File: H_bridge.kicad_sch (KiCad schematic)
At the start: 42 parts

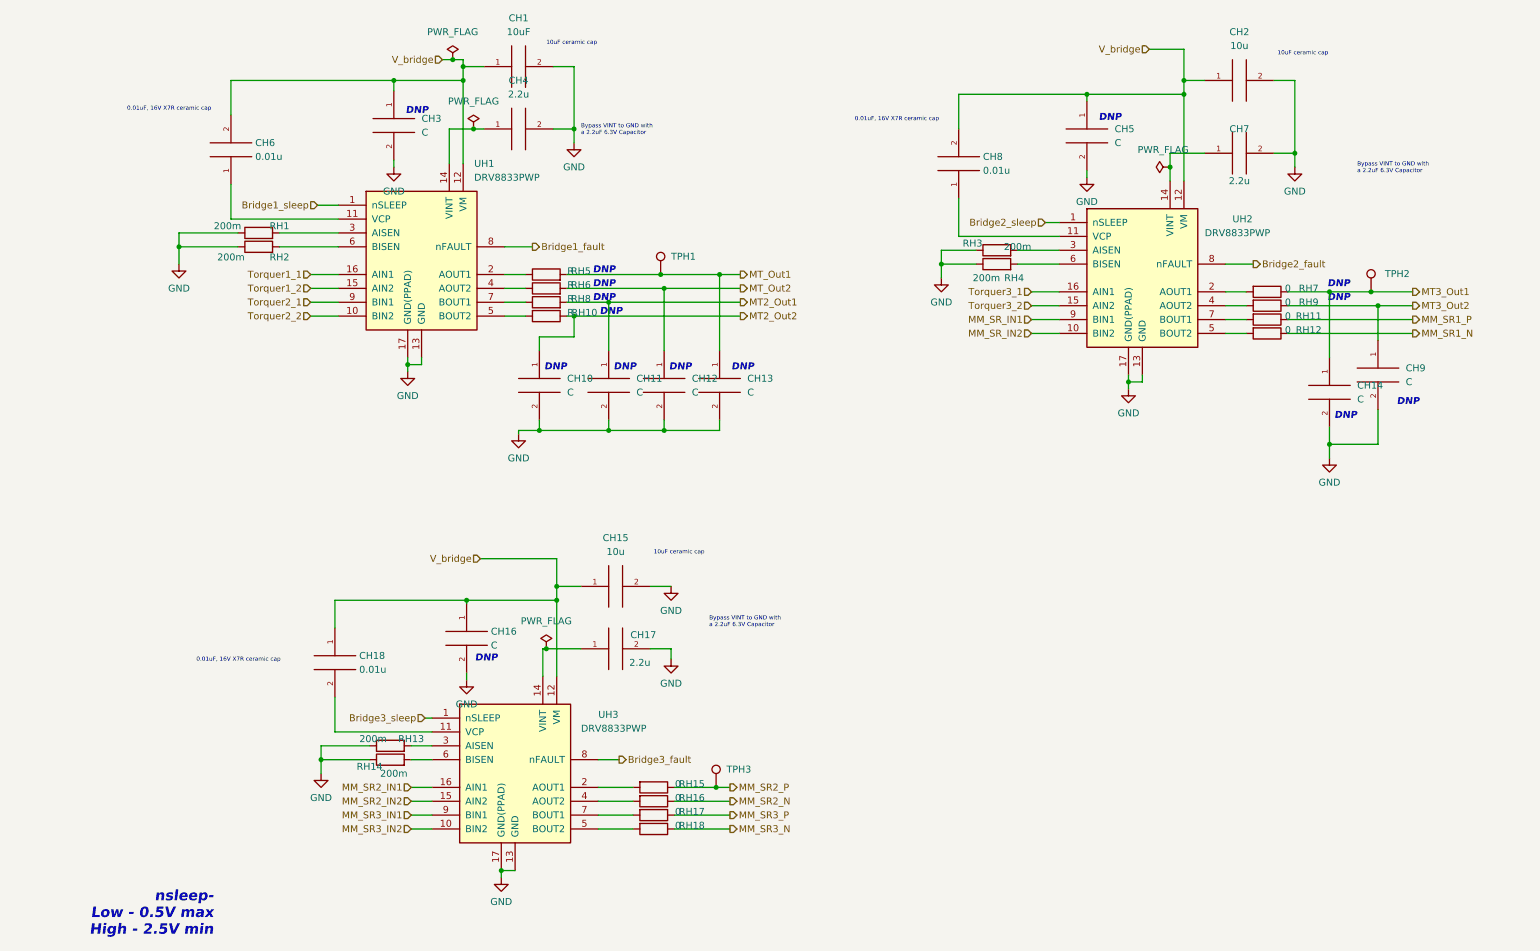
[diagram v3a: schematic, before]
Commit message: H-bridge capacitor PN added
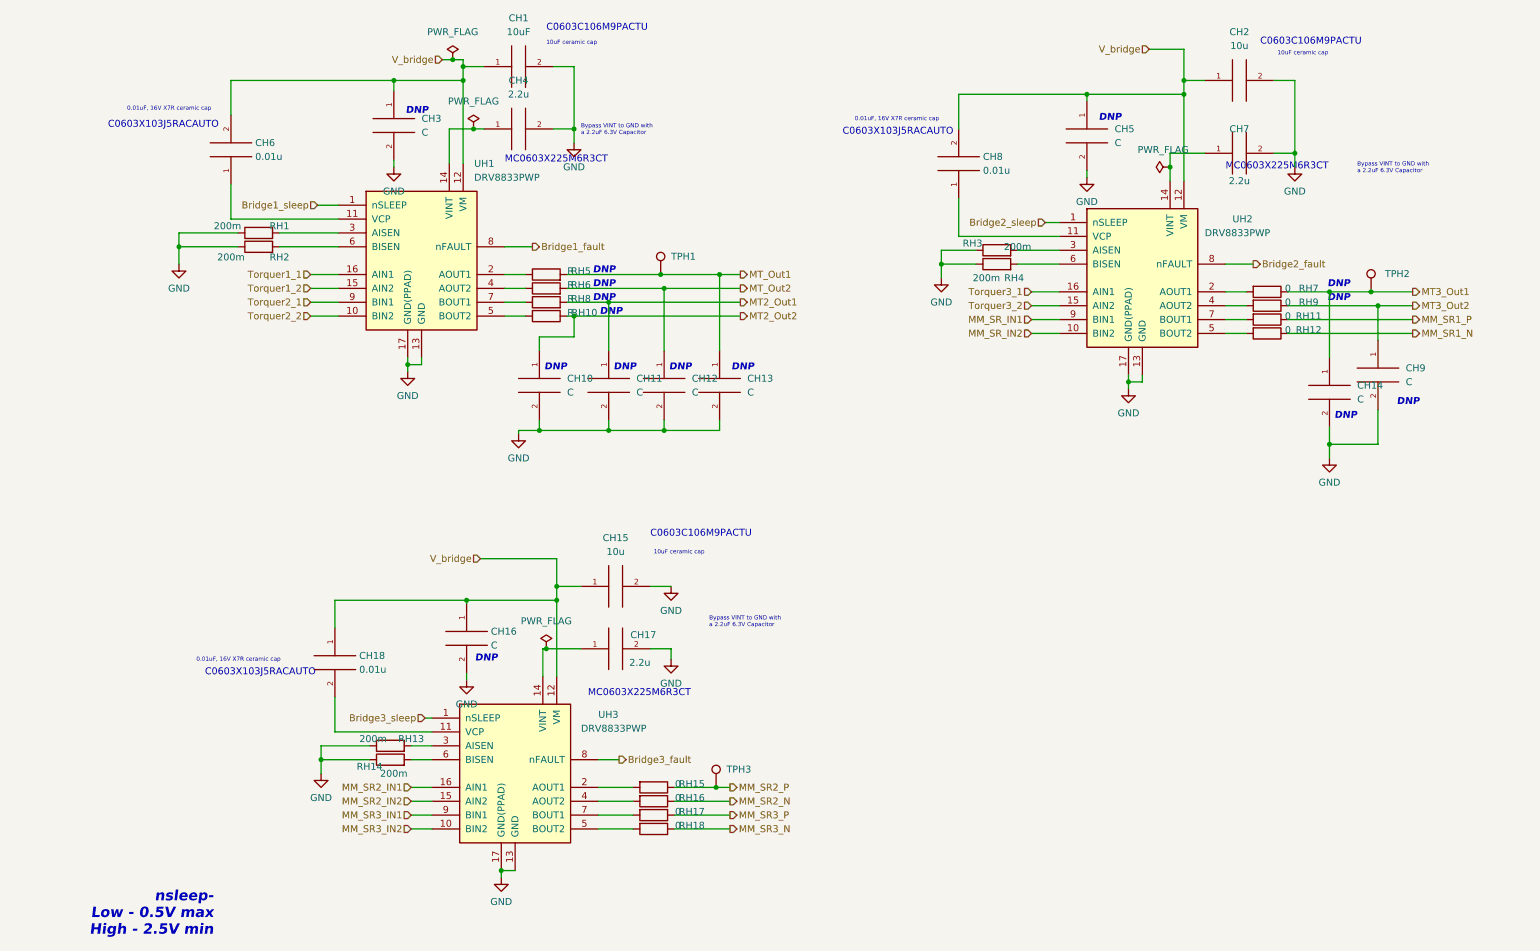
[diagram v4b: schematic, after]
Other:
- note added: "C0603C106M9PACTU"
- note added: "C0603X103J5RACAUTO"
- note added: "MC0603X225M6R3CT"
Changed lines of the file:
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@@
     (effects (font (size 0.762 0.762)) (justify left bottom))
+  )
+  (text "\n    C0603X103J5RACAUTO" (at 35.56 142.24 0)
+    (effects (font (size 1.27 1.27)) (justify left bottom))
   )
   (text "0.01uF, 16V X7R ceramic cap" (at 36.195 139.7 0)
@@
     (effects (font (size 1.27 1.27) bold italic) (justify right bottom))
   )
+  (text "\n    C0603X103J5RACAUTO" (at 152.4 43.18 0)
+    (effects (font (size 1.27 1.27)) (justify left bottom))
+  )
+  (text "C0603C106M9PACTU" (at 119.38 116.84 0)
+    (effects (font (size 1.27 1.27)) (justify left bottom))
+  )
   (text "Bypass VINT to GND with \na 2.2uF 6.3V Capacitor" (at 106.68 43.18 0)
     (effects (font (size 0.762 0.762)) (justify left bottom))
@@
   (text "Bypass VINT to GND with \na 2.2uF 6.3V Capacitor" (at 248.92 50.165 0)
     (effects (font (size 0.762 0.762)) (justify left bottom))
+  )
+  (text "C0603C106M9PACTU" (at 100.33 24.13 0)
+    (effects (font (size 1.27 1.27)) (justify left bottom))
   )
   (text "10uF ceramic cap" (at 234.315 28.575 0)
@@
     (effects (font (size 1.27 1.27) bold italic) (justify right bottom))
   )
+  (text "\n    C0603X103J5RACAUTO" (at 17.78 41.91 0)
+    (effects (font (size 1.27 1.27)) (justify left bottom))
+  )
+  (text "C0603C106M9PACTU" (at 231.14 26.67 0)
+    (effects (font (size 1.27 1.27)) (justify left bottom))
+  )
   (text "DNP" (at 138.43 86.36 180)
     (effects (font (size 1.27 1.27) bold italic) (justify right bottom))
@@
   (text "nsleep-\n	Low - 0.5V max\n	High - 2.5V min" (at 39.37 189.865 180)
     (effects (font (size 1.905 1.905) bold italic) (justify right bottom))
+  )
+  (text "MC0603X225M6R3CT " (at 224.79 49.53 0)
+    (effects (font (size 1.27 1.27)) (justify left bottom))
   )
   (text "DNP" (at 248.92 95.25 180)
@@
     (effects (font (size 1.27 1.27) bold italic) (justify right bottom))
   )
+  (text "MC0603X225M6R3CT " (at 107.95 146.05 0)
+    (effects (font (size 1.27 1.27)) (justify left bottom))
+  )
+  (text "MC0603X225M6R3CT " (at 92.71 48.26 0)
+    (effects (font (size 1.27 1.27)) (justify left bottom))
+  )
   (text "0.01uF, 16V X7R ceramic cap" (at 156.845 40.64 0)
